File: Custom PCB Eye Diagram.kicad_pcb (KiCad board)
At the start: 4 copper layers, 90.3 x 100.2 mm, 66 parts, among them IC1 DSC1123CI2-125.0000, J1 Conn_01x02, J10 PJ-102B, J11 Conn_01x02, J12 Conn_01x02, J13 47272-0001, J14 LSHM-150-XX.X-XX-DV-A-N, J15 Conn_01x02, J16 LSHM-150-XX.X-XX-DV-A-N, J17 Conn_01x02, J2 Conn_01x04, J3 Conn_01x03, J4 Conn_01x02, J5 Conn_01x04, J6 0878321420, J7 Conn_01x02, J8 Conn_01x02, J9 47272-0001, U1 OKI-78SR-3.3_1.5-W36-C

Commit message: Made changes to the LSHM footprints
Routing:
- net GND: track 82.8 -> 99.1 mm, vias 43 -> 45
- net +3V3: track 39.2 -> 35.2 mm
- net /MGT_CLK0_N: track 53.5 -> 52.1 mm
- net /MGT_CLK0_P: track 55.2 -> 53.7 mm
- net /TDO: track 22.4 -> 21.2 mm
- net /LVDS_0_P: track 73.4 -> 72.6 mm
- net /MGT_TX0_N: track 47.2 -> 46.4 mm
- net /MGT_RX3_C_P: track 42.1 -> 41.4 mm
- net /MGT_RX3_C_N: track 42.9 -> 42.2 mm
- net /MGT_RX2_C_N: track 49.8 -> 49.1 mm
- net /MGT_RX1_C_N: track 56.8 -> 56.0 mm
- net /MGT_RX0_C_P: track 63.9 -> 63.1 mm
- net Net-(J16-Pad87): track 3.83 -> 3.08 mm
- net Net-(J16-Pad81): track 5.28 -> 4.53 mm
- net Net-(J16-Pad77): track 6.67 -> 5.92 mm
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
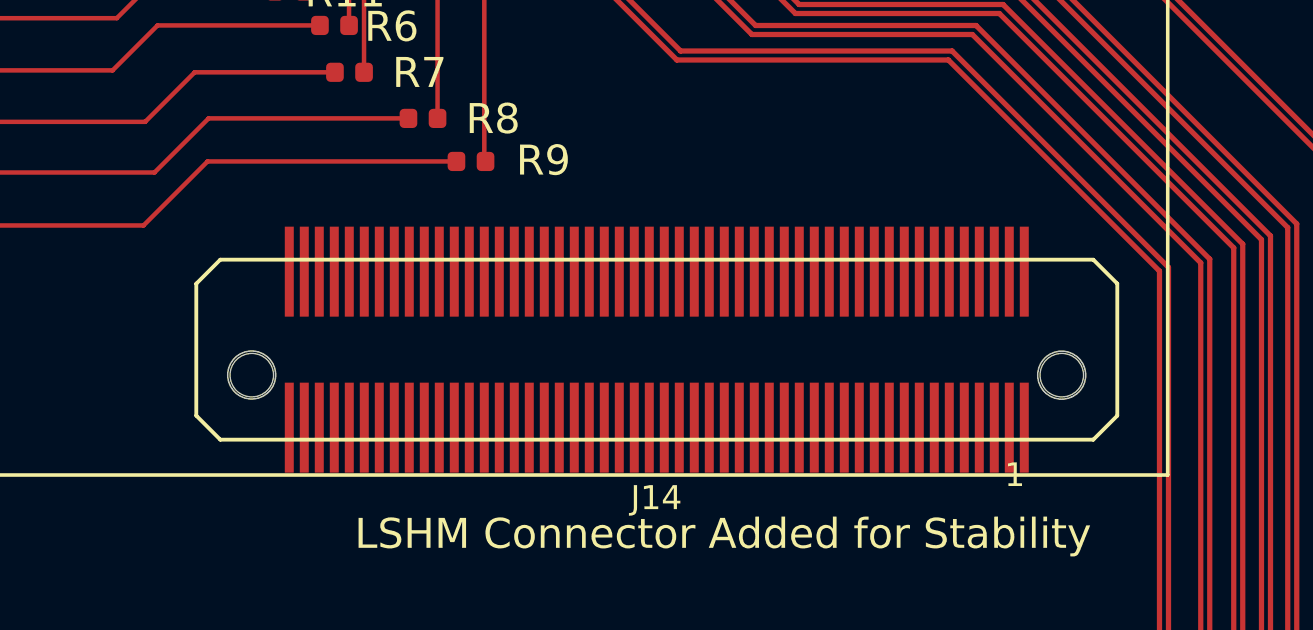
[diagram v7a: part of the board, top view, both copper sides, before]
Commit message: Further changes to LSHM connectors
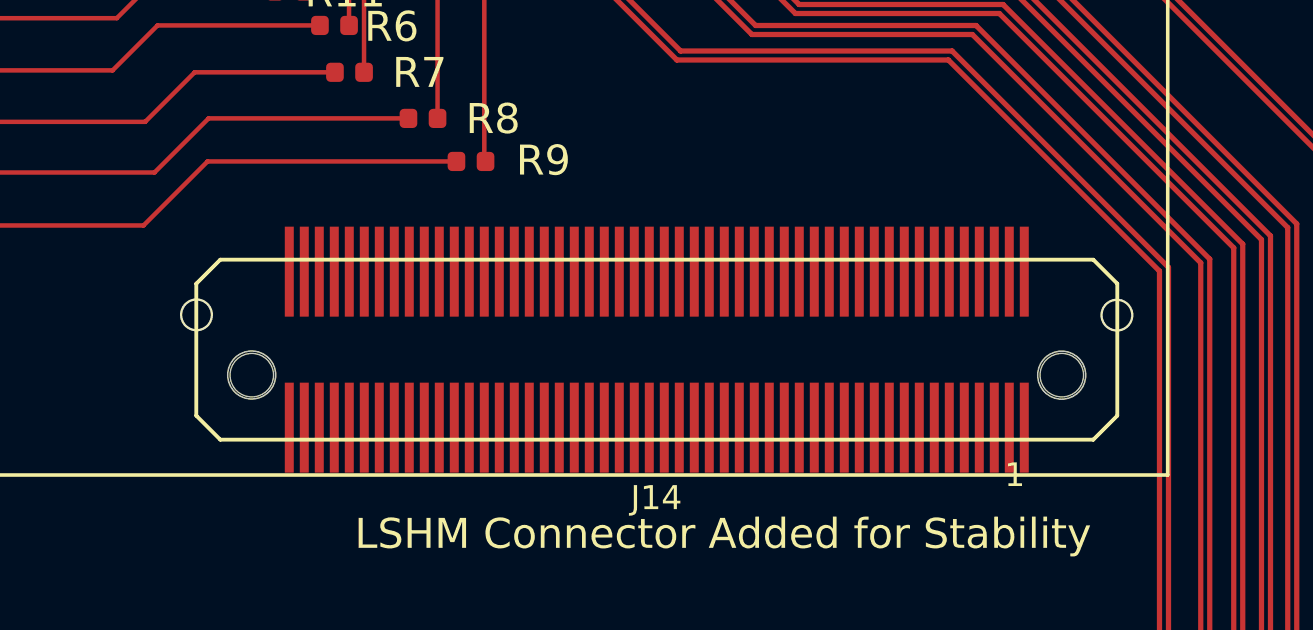
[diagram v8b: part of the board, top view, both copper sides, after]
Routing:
- net GND: vias 45 -> 47
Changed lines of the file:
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@@
     (thickness 1.6)
     (drawings 46)
-    (tracks 602)
+    (tracks 604)
     (zones 0)
     (modules 66)
@@
   (page A4)
   (layers
-    (0 F.Cu signal)
+    (0 F.Cu signal hide)
     (1 In1.Cu power hide)
     (2 In2.Cu power hide)
@@
   (via (at 157.19 74.84) (size 1.1) (drill 0.95) (layers F.Cu B.Cu) (net 1))
   (via (at 126.49 74.82) (size 1.1) (drill 0.95) (layers F.Cu B.Cu) (net 1))
+  (via (at 132.5 96.82) (size 1.1) (drill 0.95) (layers F.Cu B.Cu) (net 1))
+  (via (at 163.18 96.83) (size 1.1) (drill 0.95) (layers F.Cu B.Cu) (net 1))
   (segment (start 150.1902 117.8561) (end 153.7337 117.8561) (width 0.508) (layer F.Cu) (net 2))
   (segment (start 153.7337 117.8561) (end 153.7462 117.8686) (width 0.508) (layer F.Cu) (net 2))
